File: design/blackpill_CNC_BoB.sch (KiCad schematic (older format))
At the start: 302 parts, among them J101 ALimIN, J102 ZLimIN, J103 YLimIN, J104 XLimIN, J105 CS_IN, J106 FH_IN, J107 DoorIN, J108 ResetIN, J109 ProbeIN, J110 12V Power in, J111 AuxEncIn, J112 5V Power out, J113 ADC_in_1, J114 ADC_in_2, J115 stepDriverLim, J116 Reset, J117 UART1, J118 I2C, J119 SpindleVFD, J120 Spindle/Coolant, J121 Spindle, J122 Coolant, J123 AuxOut, J124 XStepDrv, J125 YStepDrv, J126 ZStepDrv, J127 AStepDrv, J128 Driver Power in/out, U101 TLP290-4, U102 TLP290-4, U103 TLP290-4, U104 74LVC2G17, U105 LD1117S50TR_SOT223, U106 LM358, U107 TLV9001, U108 TLV9001, U109 YAAJ_WeAct_BlackPill_Part_Like, U110 TLV9001, U111 TLV9001, U112 74HCT541, U113 74HCT541, U114 74HCT541, U115 ULN2003A, U116 ULN2003A, U117 ULN2003A

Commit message: still ... refigure driver voltage jumper
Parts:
- removed JP136: Jumper_NC_Dual, Connector_PinHeader_2.54mm:PinHeader_1x03_P2.54mm_Vertical, symbol Device:Jumper_NC_Dual
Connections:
- net Vdrive renamed V_Drive
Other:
- moved on the sheet: J128
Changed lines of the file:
@@
 Wire Wire Line
 	15400 4450 15450 4450
-$Comp
-L Nucleo64-CNC-rescue:Vdrive-power #PWR0199
-U 1 1 6CB28B07
-P 15600 2950
-F 0 "#PWR0199" H 15400 2800 50  0001 C CNN
-F 1 "Vdrive" H 15617 3123 50  0000 C CNN
-F 2 "" H 15600 2950 50  0001 C CNN
-F 3 "" H 15600 2950 50  0001 C CNN
-	1    15600 2950
-	1    0    0    -1
-$EndComp
 Wire Wire Line
 	15150 2950 15300 2950
@@
 $EndComp
 $Comp
-L Nucleo64-CNC-rescue:Vdrive-power #PWR0197
-U 1 1 6CDC2DB1
-P 15400 6000
-F 0 "#PWR0197" H 15200 5850 50  0001 C CNN
-F 1 "Vdrive" V 15417 6173 50  0001 C CNN
-F 2 "" H 15400 6000 50  0001 C CNN
-F 3 "" H 15400 6000 50  0001 C CNN
-	1    15400 6000
-	0    1    -1   0
-$EndComp
-$Comp
 L power:+5V #PWR0195
 U 1 1 6CDC2F60
@@
 	15400 5600 14900 5600
 Wire Wire Line
-	15400 6000 15000 6000
-Wire Wire Line
 	15400 5800 15200 5800
 $Comp
@@
 Wire Wire Line
 	15400 2050 15450 2050
-$Comp
-L Nucleo64-CNC-rescue:Vdrive-power #PWR0200
-U 1 1 6D77628E
-P 15800 700
-F 0 "#PWR0200" H 15600 550 50  0001 C CNN
-F 1 "Vdrive" H 15817 873 50  0000 C CNN
-F 2 "" H 15800 700 50  0001 C CNN
-F 3 "" H 15800 700 50  0001 C CNN
-	1    15800 700
-	1    0    0    -1
-$EndComp
 Wire Wire Line
 	15150 550  15300 550
@@
 	6350 6950 6350 6750
 $Comp
-L Nucleo64-CNC-rescue:Vdrive-power #PWR0132
-U 1 1 698A2D21
-P 6950 8950
-F 0 "#PWR0132" H 6750 8800 50  0001 C CNN
-F 1 "Vdrive" H 6967 9123 50  0000 C CNN
-F 2 "" H 6950 8950 50  0001 C CNN
-F 3 "" H 6950 8950 50  0001 C CNN
-	1    6950 8950
-	1    0    0    -1
-$EndComp
-$Comp
 L Connector:Screw_Terminal_01x02 J128
 U 1 1 698AEEDC
-P 7150 9300
-F 0 "J128" H 7150 9100 50  0000 C CNN
-F 1 "Driver Power in/out" V 7300 9250 50  0000 C CNN
-F 2 "Connector_Phoenix_MSTB:PhoenixContact_MSTBA_2,5_2-G-5,08_1x02_P5.08mm_Horizontal" H 7150 9300 50  0001 C CNN
-F 3 "~" H 7150 9300 50  0001 C CNN
-	1    7150 9300
+P 15750 6200
+F 0 "J128" H 15750 6000 50  0000 C CNN
+F 1 "Driver Power in/out" V 15900 6150 50  0000 C CNN
+F 2 "Connector_Phoenix_MSTB:PhoenixContact_MSTBA_2,5_2-G-5,08_1x02_P5.08mm_Horizontal" H 15750 6200 50  0001 C CNN
+F 3 "~" H 15750 6200 50  0001 C CNN
+	1    15750 6200
 	1    0    0    1
 $EndComp
 $Comp
-L power:GND #PWR0152
-U 1 1 698B07EF
-P 6950 9300
-F 0 "#PWR0152" H 6950 9050 50  0001 C CNN
-F 1 "GND" H 7000 9100 50  0001 C CNN
-F 2 "" H 6950 9300 50  0001 C CNN
-F 3 "" H 6950 9300 50  0001 C CNN
-	1    6950 9300
+L power:GND #PWR0132
+U 1 1 69B50A4B
+P 15550 6200
+F 0 "#PWR0132" H 15550 5950 50  0001 C CNN
+F 1 "GND" H 15550 6050 50  0000 C CNN
+F 2 "" H 15550 6200 50  0001 C CNN
+F 3 "" H 15550 6200 50  0001 C CNN
+	1    15550 6200
 	1    0    0    -1
 $EndComp
-$Comp
-L Device:Jumper_NC_Dual JP136
-U 1 1 698B1E24
-P 6750 9200
-F 0 "JP136" H 6750 9350 50  0000 L CNN
-F 1 "Jumper_NC_Dual" V 6750 9350 50  0001 L CNN
-F 2 "Connector_PinHeader_2.54mm:PinHeader_1x03_P2.54mm_Vertical" H 6750 9200 50  0001 C CNN
-F 3 "~" H 6750 9200 50  0001 C CNN
-	1    6750 9200
-	0    -1   -1   0
-$EndComp
-$Comp
-L power:+5V #PWR0203
-U 1 1 698C5FFC
-P 6750 9450
-F 0 "#PWR0203" H 6750 9300 50  0001 C CNN
-F 1 "+5V" V 6750 9650 50  0000 C CNN
-F 2 "" H 6750 9450 50  0001 C CNN
-F 3 "" H 6750 9450 50  0001 C CNN
-	1    6750 9450
-	0    -1   -1   0
-$EndComp
-$Comp
-L power:+12V #PWR0204
-U 1 1 698CEBA8
-P 6750 8950
-F 0 "#PWR0204" H 6750 8800 50  0001 C CNN
-F 1 "+12V" V 6750 9200 50  0000 C CNN
-F 2 "" H 6750 8950 50  0001 C CNN
-F 3 "" H 6750 8950 50  0001 C CNN
-	1    6750 8950
-	0    -1   1    0
-$EndComp
 Wire Wire Line
-	6850 9200 6950 9200
+	15550 6100 15000 6100
+Wire Wire Line
+	15000 6100 15000 6000
+Text Label 15800 700  0    50   ~ 0
+V_Drive
+Text Label 15600 2950 0    50   ~ 0
+V_Drive
+Text Label 15300 6000 0    50   ~ 0
+V_Drive
 Wire Wire Line
-	6950 9200 6950 8950
-Connection ~ 6950 9200
+	15300 6000 15000 6000
 $EndSCHEMATC

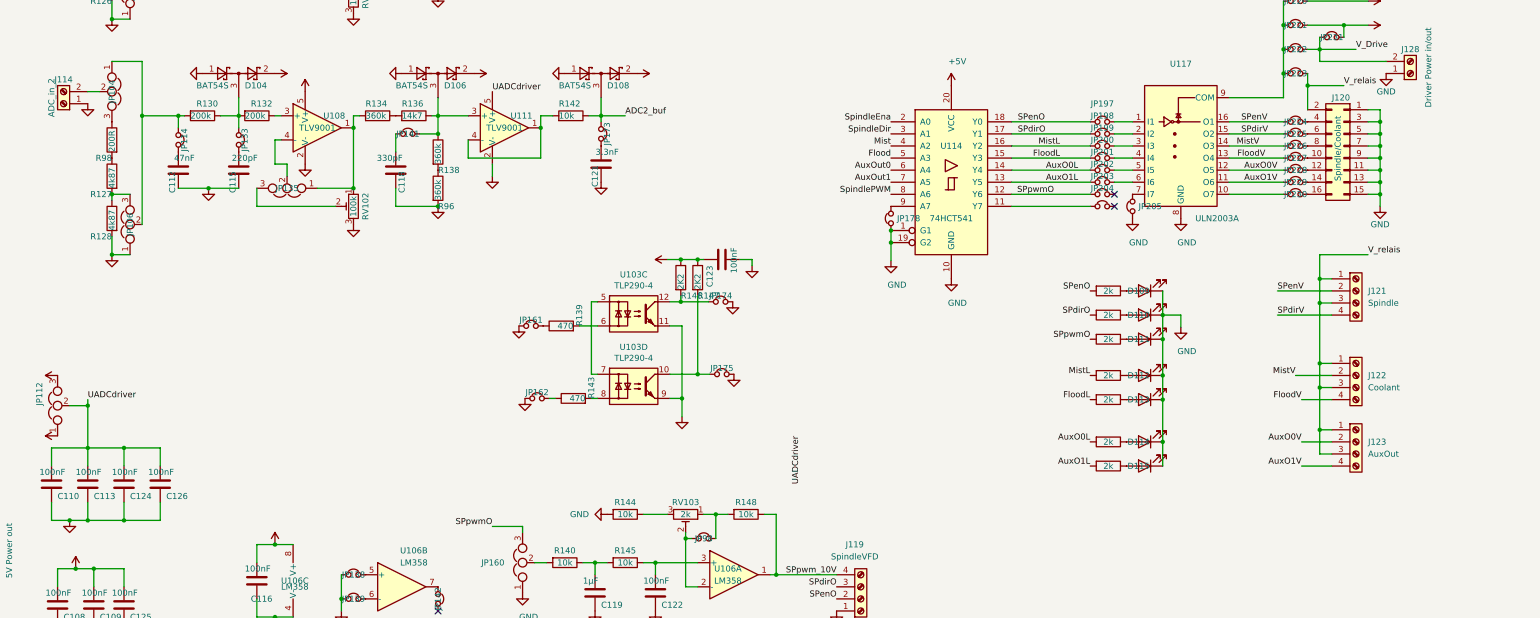
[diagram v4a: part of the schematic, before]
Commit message: arrange adc in
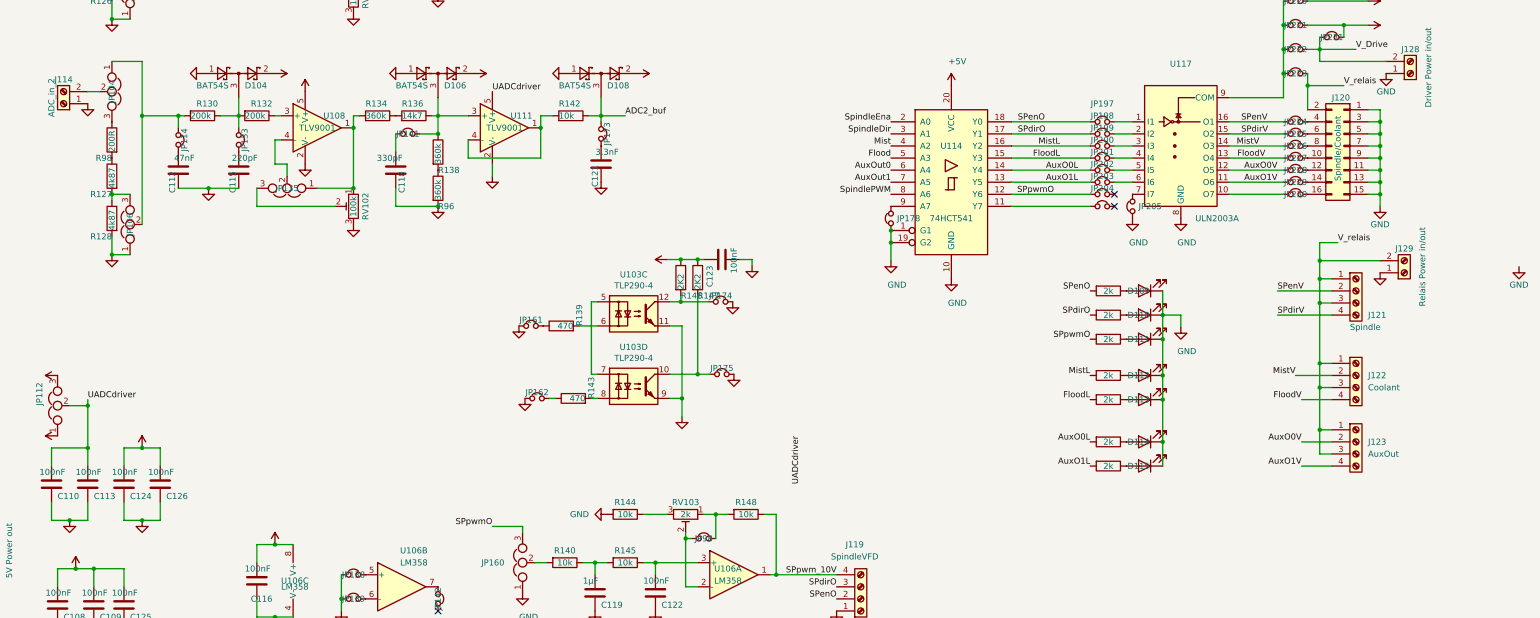
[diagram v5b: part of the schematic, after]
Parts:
- added J129: Relais Power in/out, conn_my_kf128:ScrewTerminal_1x2_P2.54mm_Vertical, symbol Connector:Screw_Terminal_01x02
- J112, J128: footprint Connector_Phoenix_MSTB:PhoenixContact_MSTBA_2,5_2-G-5,08_1x02_P5.08mm_Horizontal -> conn_my_kf128:ScrewTerminal_1x2_P2.54mm_Vertical
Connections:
- net +5V: now also C124.1, C126.1
- net GND: now also J129.1 (Pin_1)
- net UADCdriver: no longer C124.1, C126.1
- net V_relais: now also J129.2 (Pin_2)
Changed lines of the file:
@@
 Wire Wire Line
 	14900 6200 14900 6300
-Wire Wire Line
-	15200 6300 14900 6300
 Connection ~ 14900 6300
 Wire Wire Line
@@
 U 1 1 6DCCD571
 P 15300 8000
-F 0 "J121" H 15400 8000 50  0000 L CNN
-F 1 "Spindle" H 15400 7900 50  0000 L CNN
+F 0 "J121" H 15400 7800 50  0000 L CNN
+F 1 "Spindle" H 15250 7700 50  0000 L CNN
 F 2 "conn_my_kf128:ScrewTerminal_1x4_P2.54mm_Vertical" H 15300 8000 50  0001 C CNN
 F 3 "~" H 15300 8000 50  0001 C CNN
@@
 	1    0    0    -1
 $EndComp
-Text Label 15400 7700 0    50   ~ 0
+Text Label 15150 7600 0    50   ~ 0
 V_relais
 Wire Wire Line
-	15400 7700 15000 7700
-Wire Wire Line
-	15000 7700 15000 7900
-Wire Wire Line
 	15000 8800 15100 8800
 Wire Wire Line
@@
 Wire Wire Line
 	15100 7900 15000 7900
-Connection ~ 15000 7900
 Wire Wire Line
 	15000 7900 15000 8100
@@
 F 0 "J112" H 4000 10000 50  0000 C CNN
 F 1 "5V Power out" V 4150 10150 50  0000 C CNN
-F 2 "Connector_Phoenix_MSTB:PhoenixContact_MSTBA_2,5_2-G-5,08_1x02_P5.08mm_Horizontal" H 4000 10200 50  0001 C CNN
+F 2 "conn_my_kf128:ScrewTerminal_1x2_P2.54mm_Vertical" H 4000 10200 50  0001 C CNN
 F 3 "~" H 4000 10200 50  0001 C CNN
 	1    4000 10200
@@
 Connection ~ 4850 10900
 Wire Wire Line
-	4800 9900 5100 9900
-Wire Wire Line
 	5400 9900 5400 9750
-Connection ~ 4800 9900
 Wire Wire Line
 	5100 9750 5100 9900
-Connection ~ 5100 9900
-Wire Wire Line
-	5100 9900 5400 9900
 Wire Wire Line
-	4800 9300 5100 9300
+	5100 9900 5250 9900
 Wire Wire Line
 	5400 9300 5400 9450
 Wire Wire Line
 	5100 9450 5100 9300
-Connection ~ 5100 9300
 Wire Wire Line
-	5100 9300 5400 9300
+	5100 9300 5250 9300
 $Comp
 L Device:Jumper_NC_Dual JP135
@@
 F 0 "J128" H 15750 6000 50  0000 C CNN
 F 1 "Driver Power in/out" V 15900 6150 50  0000 C CNN
-F 2 "Connector_Phoenix_MSTB:PhoenixContact_MSTBA_2,5_2-G-5,08_1x02_P5.08mm_Horizontal" H 15750 6200 50  0001 C CNN
+F 2 "conn_my_kf128:ScrewTerminal_1x2_P2.54mm_Vertical" H 15750 6200 50  0001 C CNN
 F 3 "~" H 15750 6200 50  0001 C CNN
 	1    15750 6200
@@
 Wire Wire Line
 	15300 6000 15000 6000
+$Comp
+L Connector:Screw_Terminal_01x02 J129
+U 1 1 69D0FE53
+P 15700 7850
+F 0 "J129" H 15700 7650 50  0000 C CNN
+F 1 "Relais Power in/out" V 15850 7800 50  0000 C CNN
+F 2 "conn_my_kf128:ScrewTerminal_1x2_P2.54mm_Vertical" H 15700 7850 50  0001 C CNN
+F 3 "~" H 15700 7850 50  0001 C CNN
+	1    15700 7850
+	1    0    0    1
+$EndComp
+$Comp
+L power:GND #PWR0152
+U 1 1 69D9433E
+P 16650 7800
+F 0 "#PWR0152" H 16650 7550 50  0001 C CNN
+F 1 "GND" H 16650 7650 50  0000 C CNN
+F 2 "" H 16650 7800 50  0001 C CNN
+F 3 "" H 16650 7800 50  0001 C CNN
+	1    16650 7800
+	1    0    0    -1
+$EndComp
+Wire Wire Line
+	14900 6300 15200 6300
+Wire Wire Line
+	15000 7900 15000 7750
+Wire Wire Line
+	15000 7600 15150 7600
+Connection ~ 15000 7900
+$Comp
+L power:GND #PWR0197
+U 1 1 69EC8147
+P 15500 7850
+F 0 "#PWR0197" H 15500 7600 50  0001 C CNN
+F 1 "GND" H 15500 7700 50  0001 C CNN
+F 2 "" H 15500 7850 50  0001 C CNN
+F 3 "" H 15500 7850 50  0001 C CNN
+	1    15500 7850
+	1    0    0    -1
+$EndComp
+Wire Wire Line
+	15500 7750 15000 7750
+Connection ~ 15000 7750
+Wire Wire Line
+	15000 7750 15000 7600
+$Comp
+L power:GND #PWR?
+U 1 1 6A00AD7F
+P 5250 9900
+F 0 "#PWR?" H 5250 9650 50  0001 C CNN
+F 1 "GND" H 5300 9700 50  0001 C CNN
+F 2 "" H 5250 9900 50  0001 C CNN
+F 3 "" H 5250 9900 50  0001 C CNN
+	1    5250 9900
+	1    0    0    -1
+$EndComp
+Connection ~ 5250 9900
+Wire Wire Line
+	5250 9900 5400 9900
+$Comp
+L power:+5V #PWR?
+U 1 1 6A00BF5B
+P 5250 9300
+F 0 "#PWR?" H 5250 9150 50  0001 C CNN
+F 1 "+5V" H 5300 9500 50  0001 C CNN
+F 2 "" H 5250 9300 50  0001 C CNN
+F 3 "" H 5250 9300 50  0001 C CNN
+	1    5250 9300
+	1    0    0    -1
+$EndComp
+Connection ~ 5250 9300
+Wire Wire Line
+	5250 9300 5400 9300
 $EndSCHEMATC

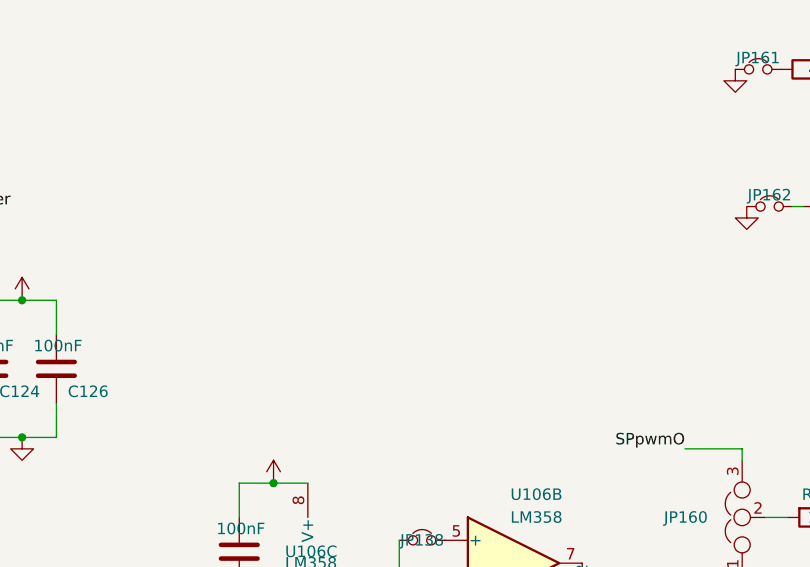
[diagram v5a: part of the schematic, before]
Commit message: added exp power pins
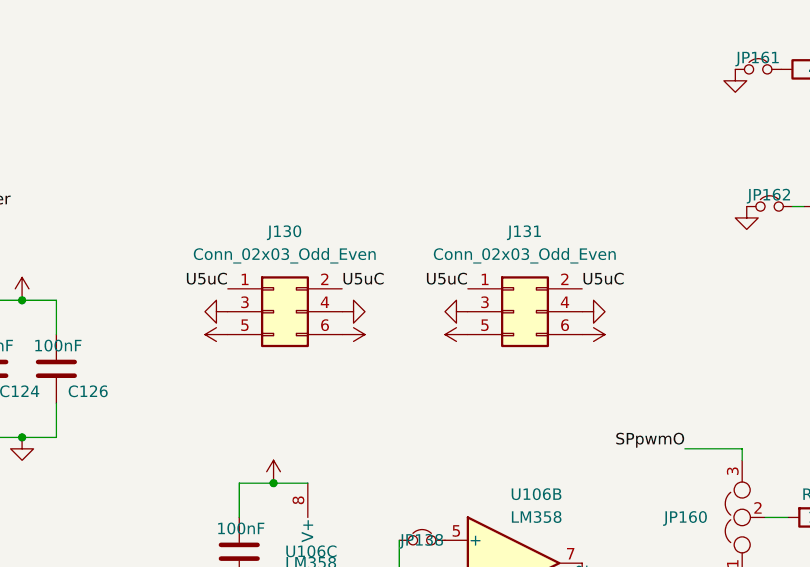
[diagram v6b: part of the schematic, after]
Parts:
- added J130, J131: Conn_02x03_Odd_Even, Connector_PinHeader_2.54mm:PinHeader_2x03_P2.54mm_Vertical, symbol Connector_Generic:Conn_02x03_Odd_Even
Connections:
- net +3V3: now also J130.5 (Pin_5), J130.6 (Pin_6), J131.5 (Pin_5), J131.6 (Pin_6)
- net GND: now also J130.3 (Pin_3), J130.4 (Pin_4), J131.3 (Pin_3), J131.4 (Pin_4)
- net U5uC: now also J130.1 (Pin_1), J130.2 (Pin_2), J131.1 (Pin_1), J131.2 (Pin_2)
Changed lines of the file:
@@
 	15000 7750 15000 7600
 $Comp
-L power:GND #PWR?
+L power:GND #PWR0199
 U 1 1 6A00AD7F
 P 5250 9900
-F 0 "#PWR?" H 5250 9650 50  0001 C CNN
+F 0 "#PWR0199" H 5250 9650 50  0001 C CNN
 F 1 "GND" H 5300 9700 50  0001 C CNN
 F 2 "" H 5250 9900 50  0001 C CNN
@@
 	5250 9900 5400 9900
 $Comp
-L power:+5V #PWR?
+L power:+5V #PWR0200
 U 1 1 6A00BF5B
 P 5250 9300
-F 0 "#PWR?" H 5250 9150 50  0001 C CNN
+F 0 "#PWR0200" H 5250 9150 50  0001 C CNN
 F 1 "+5V" H 5300 9500 50  0001 C CNN
 F 2 "" H 5250 9300 50  0001 C CNN
@@
 Wire Wire Line
 	5250 9300 5400 9300
+$Comp
+L Connector_Generic:Conn_02x03_Odd_Even J130
+U 1 1 6A3E047F
+P 6350 9350
+F 0 "J130" H 6400 9700 50  0000 C CNN
+F 1 "Conn_02x03_Odd_Even" H 6400 9600 50  0000 C CNN
+F 2 "Connector_PinHeader_2.54mm:PinHeader_2x03_P2.54mm_Vertical" H 6350 9350 50  0001 C CNN
+F 3 "~" H 6350 9350 50  0001 C CNN
+	1    6350 9350
+	1    0    0    -1
+$EndComp
+$Comp
+L power:+3.3V #PWR0204
+U 1 1 6A40F7FA
+P 6150 9450
+F 0 "#PWR0204" H 6150 9300 50  0001 C CNN
+F 1 "+3.3V" H 6165 9623 50  0001 C CNN
+F 2 "" H 6150 9450 50  0001 C CNN
+F 3 "" H 6150 9450 50  0001 C CNN
+	1    6150 9450
+	0    -1   -1   0
+$EndComp
+$Comp
+L power:GND #PWR0203
+U 1 1 6A41063C
+P 6150 9350
+F 0 "#PWR0203" H 6150 9100 50  0001 C CNN
+F 1 "GND" H 6200 9150 50  0001 C CNN
+F 2 "" H 6150 9350 50  0001 C CNN
+F 3 "" H 6150 9350 50  0001 C CNN
+	1    6150 9350
+	0    1    1    0
+$EndComp
+$Comp
+L power:GND #PWR0205
+U 1 1 6A4124C7
+P 6650 9350
+F 0 "#PWR0205" H 6650 9100 50  0001 C CNN
+F 1 "GND" H 6700 9150 50  0001 C CNN
+F 2 "" H 6650 9350 50  0001 C CNN
+F 3 "" H 6650 9350 50  0001 C CNN
+	1    6650 9350
+	0    -1   -1   0
+$EndComp
+$Comp
+L power:+3.3V #PWR0206
+U 1 1 6A513EEA
+P 6650 9450
+F 0 "#PWR0206" H 6650 9300 50  0001 C CNN
+F 1 "+3.3V" H 6665 9623 50  0001 C CNN
+F 2 "" H 6650 9450 50  0001 C CNN
+F 3 "" H 6650 9450 50  0001 C CNN
+	1    6650 9450
+	0    1    1    0
+$EndComp
+Text Label 6650 9250 0    50   ~ 0
+U5uC
+Text Label 6150 9250 2    50   ~ 0
+U5uC
+$Comp
+L Connector_Generic:Conn_02x03_Odd_Even J131
+U 1 1 6A53B75F
+P 7400 9350
+F 0 "J131" H 7450 9700 50  0000 C CNN
+F 1 "Conn_02x03_Odd_Even" H 7450 9600 50  0000 C CNN
+F 2 "Connector_PinHeader_2.54mm:PinHeader_2x03_P2.54mm_Vertical" H 7400 9350 50  0001 C CNN
+F 3 "~" H 7400 9350 50  0001 C CNN
+	1    7400 9350
+	1    0    0    -1
+$EndComp
+$Comp
+L power:+3.3V #PWR0208
+U 1 1 6A53B765
+P 7200 9450
+F 0 "#PWR0208" H 7200 9300 50  0001 C CNN
+F 1 "+3.3V" H 7215 9623 50  0001 C CNN
+F 2 "" H 7200 9450 50  0001 C CNN
+F 3 "" H 7200 9450 50  0001 C CNN
+	1    7200 9450
+	0    -1   -1   0
+$EndComp
+$Comp
+L power:GND #PWR0207
+U 1 1 6A53B76B
+P 7200 9350
+F 0 "#PWR0207" H 7200 9100 50  0001 C CNN
+F 1 "GND" H 7250 9150 50  0001 C CNN
+F 2 "" H 7200 9350 50  0001 C CNN
+F 3 "" H 7200 9350 50  0001 C CNN
+	1    7200 9350
+	0    1    1    0
+$EndComp
+$Comp
+L power:GND #PWR0209
+U 1 1 6A53B771
+P 7700 9350
+F 0 "#PWR0209" H 7700 9100 50  0001 C CNN
+F 1 "GND" H 7750 9150 50  0001 C CNN
+F 2 "" H 7700 9350 50  0001 C CNN
+F 3 "" H 7700 9350 50  0001 C CNN
+	1    7700 9350
+	0    -1   -1   0
+$EndComp
+$Comp
+L power:+3.3V #PWR0210
+U 1 1 6A53B777
+P 7700 9450
+F 0 "#PWR0210" H 7700 9300 50  0001 C CNN
+F 1 "+3.3V" H 7715 9623 50  0001 C CNN
+F 2 "" H 7700 9450 50  0001 C CNN
+F 3 "" H 7700 9450 50  0001 C CNN
+	1    7700 9450
+	0    1    1    0
+$EndComp
+Text Label 7700 9250 0    50   ~ 0
+U5uC
+Text Label 7200 9250 2    50   ~ 0
+U5uC
 $EndSCHEMATC

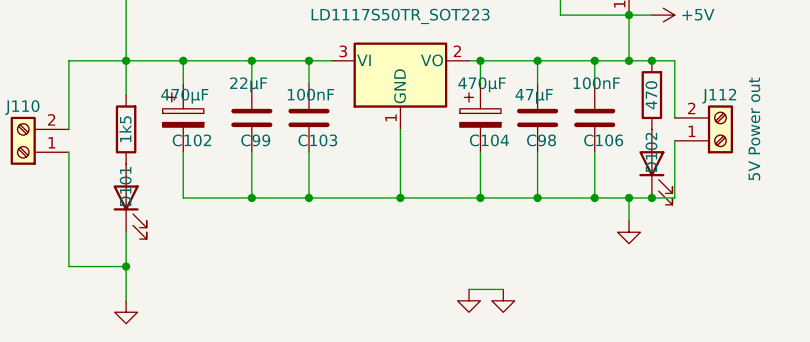
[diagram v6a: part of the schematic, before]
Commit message: placed mount holes
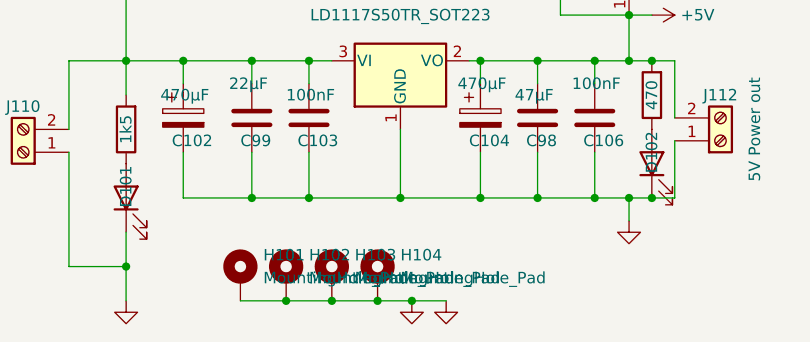
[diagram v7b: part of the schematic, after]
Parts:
- added H101, H102, H103, H104: MountingHole_Pad, MountingHole:MountingHole_3.2mm_M3_Pad, symbol Mechanical:MountingHole_Pad
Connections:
- net GND: now also H101.1, H102.1, H103.1, H104.1
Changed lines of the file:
@@
 L power:GNDS #PWR0201
 U 1 1 67D8B4F1
-P 2900 10850
-F 0 "#PWR0201" H 2900 10600 50  0001 C CNN
-F 1 "GNDS" H 2905 10677 50  0001 C CNN
-F 2 "" H 2900 10850 50  0001 C CNN
-F 3 "" H 2900 10850 50  0001 C CNN
-	1    2900 10850
+P 2650 10900
+F 0 "#PWR0201" H 2650 10650 50  0001 C CNN
+F 1 "GNDS" H 2655 10727 50  0001 C CNN
+F 2 "" H 2650 10900 50  0001 C CNN
+F 3 "" H 2650 10900 50  0001 C CNN
+	1    2650 10900
 	1    0    0    -1
 $EndComp
@@
 L power:GND #PWR0202
 U 1 1 67DBA7B6
-P 3050 10850
-F 0 "#PWR0202" H 3050 10600 50  0001 C CNN
-F 1 "GND" H 3100 10650 50  0001 C CNN
-F 2 "" H 3050 10850 50  0001 C CNN
-F 3 "" H 3050 10850 50  0001 C CNN
-	1    3050 10850
-	1    0    0    -1
-$EndComp
-Wire Wire Line
-	2900 10850 3050 10850
+P 2800 10900
+F 0 "#PWR0202" H 2800 10650 50  0001 C CNN
+F 1 "GND" H 2850 10700 50  0001 C CNN
+F 2 "" H 2800 10900 50  0001 C CNN
+F 3 "" H 2800 10900 50  0001 C CNN
+	1    2800 10900
+	1    0    0    -1
+$EndComp
+Wire Wire Line
+	2650 10900 2800 10900
 $Comp
 L Diode:1N5819 D120
@@
 Text Label 7200 9250 2    50   ~ 0
 U5uC
+$Comp
+L Mechanical:MountingHole_Pad H101
+U 1 1 6A876809
+P 1900 10800
+F 0 "H101" H 2000 10900 50  0000 L CNN
+F 1 "MountingHole_Pad" H 2000 10800 50  0000 L CNN
+F 2 "MountingHole:MountingHole_3.2mm_M3_Pad" H 1900 10800 50  0001 C CNN
+F 3 "~" H 1900 10800 50  0001 C CNN
+	1    1900 10800
+	1    0    0    -1
+$EndComp
+$Comp
+L Mechanical:MountingHole_Pad H102
+U 1 1 6A879865
+P 2100 10800
+F 0 "H102" H 2200 10900 50  0000 L CNN
+F 1 "MountingHole_Pad" H 2200 10800 50  0000 L CNN
+F 2 "MountingHole:MountingHole_3.2mm_M3_Pad" H 2100 10800 50  0001 C CNN
+F 3 "~" H 2100 10800 50  0001 C CNN
+	1    2100 10800
+	1    0    0    -1
+$EndComp
+$Comp
+L Mechanical:MountingHole_Pad H103
+U 1 1 6A8FA97E
+P 2300 10800
+F 0 "H103" H 2400 10900 50  0000 L CNN
+F 1 "MountingHole_Pad" H 2400 10800 50  0000 L CNN
+F 2 "MountingHole:MountingHole_3.2mm_M3_Pad" H 2300 10800 50  0001 C CNN
+F 3 "~" H 2300 10800 50  0001 C CNN
+	1    2300 10800
+	1    0    0    -1
+$EndComp
+$Comp
+L Mechanical:MountingHole_Pad H104
+U 1 1 6A97A3E9
+P 2500 10800
+F 0 "H104" H 2600 10900 50  0000 L CNN
+F 1 "MountingHole_Pad" H 2600 10800 50  0000 L CNN
+F 2 "MountingHole:MountingHole_3.2mm_M3_Pad" H 2500 10800 50  0001 C CNN
+F 3 "~" H 2500 10800 50  0001 C CNN
+	1    2500 10800
+	1    0    0    -1
+$EndComp
+Wire Wire Line
+	1900 10900 2100 10900
+Connection ~ 2650 10900
+Connection ~ 2100 10900
+Wire Wire Line
+	2100 10900 2300 10900
+Connection ~ 2300 10900
+Wire Wire Line
+	2300 10900 2500 10900
+Connection ~ 2500 10900
+Wire Wire Line
+	2500 10900 2650 10900
 $EndSCHEMATC
